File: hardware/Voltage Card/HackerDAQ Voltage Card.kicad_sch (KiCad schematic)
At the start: 21 parts, among them J1 0039301040, J2 0039301040, J3 0039301040, J4 0039301040, J5 0039301040, J6 0039301040, J7 0039301040, J8 0039301040, U2 OPA310xDBV

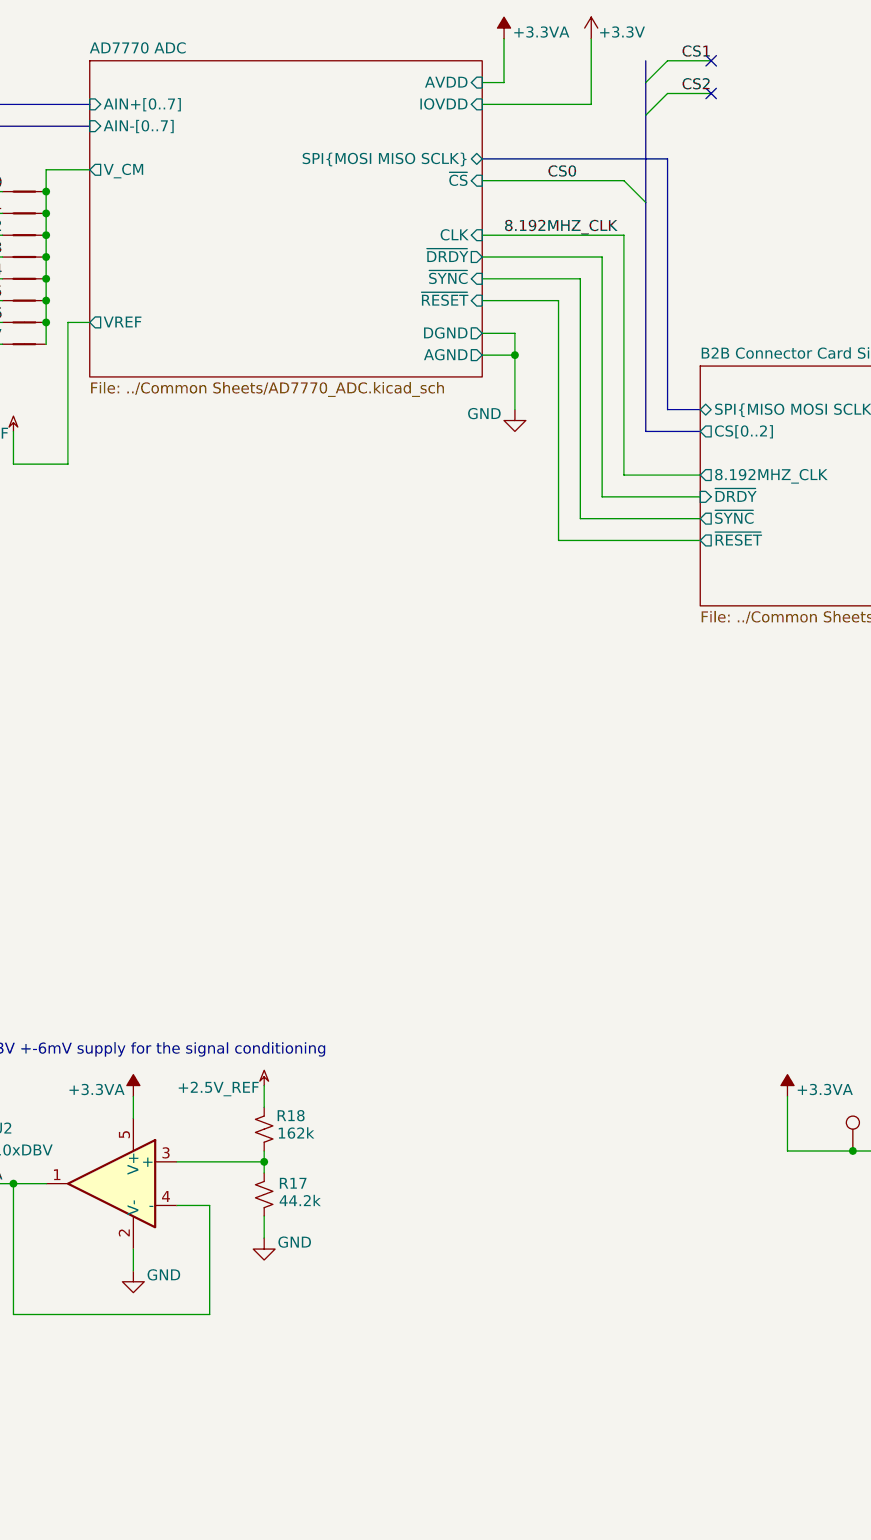
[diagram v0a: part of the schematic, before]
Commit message: Finish initial voltage card design, add logo
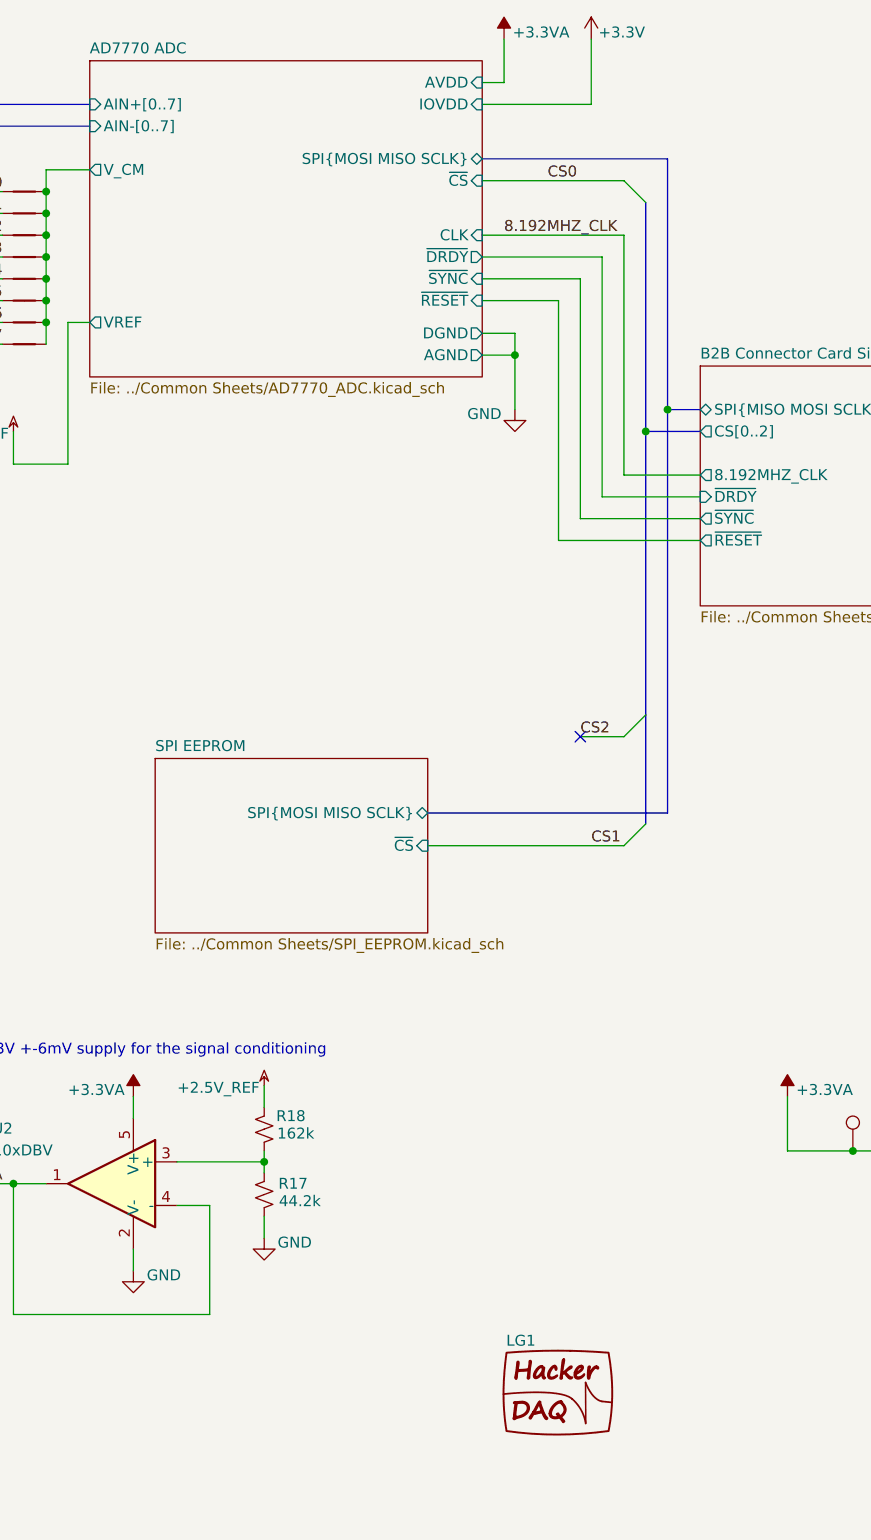
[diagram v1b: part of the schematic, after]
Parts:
- added LG1: ~, Project Library:HackerDAQ Logo, symbol Project Library:HackerDAQ_Logo
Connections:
- no-connect marks 10 -> 9
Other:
- added sheet SPI EEPROM (../Common Sheets/SPI_EEPROM.kicad_sch)
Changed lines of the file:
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@@
 	)
 	(junction
+		(at 196.85 62.23)
+		(diameter 0)
+		(color 0 0 0 0)
+	)
+	(junction
 		(at 123.19 149.86)
 		(diameter 0)
@@
 	)
 	(junction
+		(at 199.39 59.69)
+		(diameter 0)
+		(color 0 0 0 0)
+	)
+	(junction
 		(at 181.61 53.34)
 		(diameter 0)
@@
 	)
 	(no_connect
-		(at 204.47 19.05)
+		(at 189.23 97.79)
 	)
 	(no_connect
@@
 	)
 	(no_connect
-		(at 204.47 22.86)
-	)
-	(no_connect
 		(at 22.86 52.07)
 	)
@@
 	)
 	(bus_entry
-		(at 104.14 133.35)
+		(at 196.85 107.95)
 		(size -2.54 2.54)
 		(stroke
@@
 	)
 	(bus_entry
-		(at 110.49 31.75)
-		(size 2.54 2.54)
+		(at 104.14 133.35)
+		(size -2.54 2.54)
 		(stroke
 			(width 0)
@@
 	)
 	(bus_entry
-		(at 196.85 21.59)
-		(size 2.54 -2.54)
+		(at 110.49 31.75)
+		(size 2.54 2.54)
 		(stroke
 			(width 0)
@@
 	)
 	(bus_entry
-		(at 196.85 25.4)
-		(size 2.54 -2.54)
+		(at 196.85 95.25)
+		(size -2.54 2.54)
 		(stroke
 			(width 0)
@@
 		)
 	)
-	(bus
-		(pts
-			(xy 196.85 21.59) (xy 196.85 25.4)
-		)
-		(stroke
-			(width 0)
-			(type default)
-		)
-	)
 	(wire
 		(pts
@@
 		)
 	)
+	(bus
+		(pts
+			(xy 199.39 59.69) (xy 199.39 106.68)
+		)
+		(stroke
+			(width 0)
+			(type default)
+		)
+	)
 	(wire
 		(pts
@@
 		)
 	)
+	(bus
+		(pts
+			(xy 196.85 95.25) (xy 196.85 107.95)
+		)
+		(stroke
+			(width 0)
+			(type default)
+		)
+	)
 	(wire
 		(pts
@@
 	(bus
 		(pts
-			(xy 196.85 19.05) (xy 196.85 21.59)
-		)
-		(stroke
-			(width 0)
-			(type default)
-		)
-	)
-	(bus
-		(pts
 			(xy 104.14 179.07) (xy 104.14 182.88)
 		)
@@
 	(bus
 		(pts
-			(xy 196.85 25.4) (xy 196.85 35.56)
+			(xy 199.39 59.69) (xy 199.39 30.48)
 		)
 		(stroke
@@
 		)
 	)
-	(bus
+	(wire
 		(pts
-			(xy 199.39 59.69) (xy 199.39 30.48)
+			(xy 194.31 97.79) (xy 189.23 97.79)
 		)
 		(stroke
@@
 		)
 	)
-	(wire
+	(bus
 		(pts
-			(xy 82.55 109.22) (xy 96.52 109.22)
+			(xy 199.39 106.68) (xy 171.45 106.68)
 		)
 		(stroke
@@
 	(wire
 		(pts
-			(xy 254 139.7) (xy 254 149.86)
+			(xy 82.55 109.22) (xy 96.52 109.22)
 		)
 		(stroke
@@
 	(wire
 		(pts
-			(xy 19.05 45.72) (xy 19.05 49.53)
+			(xy 254 139.7) (xy 254 149.86)
 		)
 		(stroke
@@
 	(wire
 		(pts
-			(xy 19.05 135.89) (xy 22.86 135.89)
+			(xy 19.05 45.72) (xy 19.05 49.53)
 		)
 		(stroke
@@
 	(wire
 		(pts
-			(xy 113.03 44.45) (xy 121.92 44.45)
+			(xy 19.05 135.89) (xy 22.86 135.89)
 		)
 		(stroke
@@
 	(wire
 		(pts
-			(xy 199.39 19.05) (xy 204.47 19.05)
+			(xy 113.03 44.45) (xy 121.92 44.45)
 		)
 		(stroke
@@
 		)
 	)
-	(wire
-		(pts
-			(xy 199.39 22.86) (xy 204.47 22.86)
-		)
-		(stroke
-			(width 0)
-			(type default)
-		)
-	)
 	(bus
 		(pts
@@
 	(wire
 		(pts
+			(xy 171.45 110.49) (xy 194.31 110.49)
+		)
+		(stroke
+			(width 0)
+			(type default)
+		)
+	)
+	(wire
+		(pts
 			(xy 152.4 147.32) (xy 152.4 148.59)
 		)
@@
 	(bus
 		(pts
+			(xy 196.85 62.23) (xy 196.85 95.25)
+		)
+		(stroke
+			(width 0)
+			(type default)
+		)
+	)
+	(bus
+		(pts
 			(xy 110.49 41.91) (xy 110.49 44.45)
 		)
@@
 		)
 	)
+	(label "CS2"
+		(at 189.23 97.79 0)
+		(effects
+			(font
+				(size 1.27 1.27)
+			)
+			(justify left bottom)
+		)
+	)
 	(label "AIN-5"
 		(at 121.92 46.99 180)
@@
 		)
 	)
+	(label "CS1"
+		(at 190.5 110.49 0)
+		(effects
+			(font
+				(size 1.27 1.27)
+			)
+			(justify left bottom)
+		)
+	)
 	(label "8.192MHZ_CLK"
 		(at 180.34 39.37 0)
@@
 		)
 	)
-	(label "CS1"
-		(at 204.47 19.05 180)
-		(effects
-			(font
-				(size 1.27 1.27)
-			)
-			(justify right bottom)
-		)
-	)
 	(label "AIN+0"
 		(at 83.82 27.94 0)
@@
 		)
 	)
-	(label "CS2"
-		(at 204.47 22.86 180)
-		(effects
-			(font
-				(size 1.27 1.27)
-			)
-			(justify right bottom)
-		)
-	)
 	(label "CS0"
 		(at 185.42 33.02 0)
@@
 	)
 	(symbol
+		(lib_id "Project Library:HackerDAQ_Logo")
+		(at 184.15 170.18 0)
+		(unit 1)
+		(exclude_from_sim no)
+		(in_bom no)
+		(on_board yes)
+		(dnp no)
+		(property "Reference" "LG1"
+			(at 180.594 168.148 0)
+			(effects
+				(font
+					(size 1.27 1.27)
+				)
+				(justify left)
+			)
+		)
+		(property "Value" "~"
+			(at 184.15 170.18 0)
+			(effects
+				(font
+					(size 1.27 1.27)
+				)
+				(hide yes)
+			)
+		)
+		(property "Footprint" "Project Library:HackerDAQ Logo"
+			(at 195.326 165.1 0)
+			(effects
+				(font
+					(size 1.27 1.27)
+				)
+				(hide yes)
+			)
+		)
+		(property "Datasheet" ""
+			(at 184.15 170.18 0)
+			(effects
+				(font
+					(size 1.27 1.27)
+				)
+				(hide yes)
+			)
+		)
+		(property "Description" ""
+			(at 184.15 170.18 0)
+			(effects
+				(font
+					(size 1.27 1.27)
+				)
+				(hide yes)
+			)
+		)
+		(instances
+			(project ""
+				(path "/af2d881c-6553-449d-9093-6deb41497bdc"
+					(reference "LG1")
+					(unit 1)
+				)
+			)
+		)
+	)
+	(symbol
 		(lib_id "power:GND")
 		(at 39.37 162.56 0)
@@
 				)
 			)
+		)
+	)
+	(sheet
+		(at 139.7 100.33)
+		(size 31.75 20.32)
+		(exclude_from_sim no)
+		(in_bom yes)
+		(on_board yes)
+		(dnp no)
+		(fields_autoplaced yes)
+		(stroke
+			(width 0.1524)
+			(type solid)
+		)
+		(fill
+			(color 0 0 0 0.0000)
+		)
+		(property "Sheetname" "SPI EEPROM"
+			(at 139.7 99.6184 0)
+			(effects
+				(font
+					(size 1.27 1.27)
+				)
+				(justify left bottom)
+			)
+		)
+		(property "Sheetfile" "../Common Sheets/SPI_EEPROM.kicad_sch"
+			(at 139.7 121.2346 0)
+			(effects
+				(font
+					(size 1.27 1.27)
+				)
+				(justify left top)
+			)
+		)
+		(pin "SPI{MOSI MISO SCLK}" bidirectional
+			(at 171.45 106.68 0)
+			(effects
+				(font
+					(size 1.27 1.27)
+				)
+				(justify right)
+			)
+		)
+		(pin "~{CS}" input
+			(at 171.45 110.49 0)
+			(effects
+				(font
+					(size 1.27 1.27)
+				)
+				(justify right)
+			)
+		)
+		(instances
+			(project "HackerDAQ Voltage Card"
+				(path "/af2d881c-6553-449d-9093-6deb41497bdc"
+					(page "13")
+				)
+			)

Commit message: Start on MCU symbol and main unit
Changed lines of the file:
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@@
 		)
 	)
-	(label "CS2"
+	(label "CS1"
 		(at 189.23 97.79 0)
 		(effects
@@
 		)
 	)
-	(label "CS1"
+	(label "CS2"
 		(at 190.5 110.49 0)
 		(effects

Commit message: Main unit: Add USB port for MCU and 3.3VA rail, start on routing
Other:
- sheet 5V To 3.3V LDO ports: added EN; removed none
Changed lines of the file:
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@@
 	)
 	(junction
+		(at 254 147.32)
+		(diameter 0)
+		(color 0 0 0 0)
+	)
+	(junction
 		(at 152.4 147.32)
 		(diameter 0)
@@
 	(wire
 		(pts
+			(xy 254 147.32) (xy 254 149.86)
+		)
+		(stroke
+			(width 0)
+			(type default)
+		)
+	)
+	(wire
+		(pts
 			(xy 96.52 66.04) (xy 96.52 87.63)
 		)
@@
 	(wire
 		(pts
+			(xy 250.19 147.32) (xy 254 147.32)
+		)
+		(stroke
+			(width 0)
+			(type default)
+		)
+	)
+	(wire
+		(pts
 			(xy 152.4 147.32) (xy 142.24 147.32)
 		)
@@
 	(wire
 		(pts
-			(xy 254 139.7) (xy 254 149.86)
+			(xy 254 139.7) (xy 254 147.32)
 		)
 		(stroke
@@
 			)
 		)
+		(pin "EN" input
+			(at 250.19 147.32 0)
+			(effects
+				(font
+					(size 1.27 1.27)
+				)
+				(justify right)
+			)
+		)

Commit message: Route more of main unit, start on KiBot CI job
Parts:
- J1, J2, J3, J4, J5, J6, J7, J8: Mating Connector (none) -> Molex Part #39013045
- renumbered NT5 to NT2, NT2 to NT3, NT6 to NT4, NT3 to NT5, NT7 to NT6, NT4 to NT7, R18 to R17, R17 to R18, TP4 to TP1, TP5 to TP2, U2 to U1
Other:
- sheet SPI EEPROM ports: added V_{CC}; removed none
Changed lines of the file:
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@@
 	(wire
 		(pts
+			(xy 133.35 100.33) (xy 133.35 102.87)
+		)
+		(stroke
+			(width 0)
+			(type default)
+		)
+	)
+	(wire
+		(pts
 			(xy 82.55 22.86) (xy 96.52 22.86)
 		)
@@
 	(wire
 		(pts
+			(xy 133.35 102.87) (xy 139.7 102.87)
+		)
+		(stroke
+			(width 0)
+			(type default)
+		)
+	)
+	(wire
+		(pts
 			(xy 177.8 53.34) (xy 181.61 53.34)
 		)
@@
 			)
 		)
-		(property "Mating Connector" ""
+		(property "Mating Connector" "Molex Part #39013045"
 			(at 30.48 73.66 0)
 			(effects
@@
 		(dnp no)
 		(fields_autoplaced yes)
-		(property "Reference" "NT4"
+		(property "Reference" "NT7"
 			(at 124.46 36.83 0)
 			(effects
@@
 			(project "HackerDAQ Voltage Card"
 				(path "/af2d881c-6553-449d-9093-6deb41497bdc"
-					(reference "NT4")
+					(reference "NT7")
+					(unit 1)
+				)
+			)
+		)
+	)
+	(symbol
+		(lib_id "power:+8V")
+		(at 133.35 100.33 0)
+		(unit 1)
+		(exclude_from_sim no)
+		(in_bom yes)
+		(on_board yes)
+		(dnp no)
+		(property "Reference" "#PWR048"
+			(at 133.35 104.14 0)
+			(effects
+				(font
+					(size 1.27 1.27)
+				)
+				(hide yes)
+			)
+		)
+		(property "Value" "+3.3V"
+			(at 133.35 96.52 0)
+			(effects
+				(font
+					(size 1.27 1.27)
+				)
+			)
+		)
+		(property "Footprint" ""
+			(at 133.35 100.33 0)
+			(effects
+				(font
+					(size 1.27 1.27)
+				)
+				(hide yes)
+			)
+		)
+		(property "Datasheet" ""
+			(at 133.35 100.33 0)
+			(effects
+				(font
+					(size 1.27 1.27)
+				)
+				(hide yes)
+			)
+		)
+		(property "Description" "Power symbol creates a global label with name \"+8V\""
+			(at 133.35 100.33 0)
+			(effects
+				(font
+					(size 1.27 1.27)
+				)
+				(hide yes)
+			)
+		)
+		(pin "1"
+		)
+		(instances
+			(project "HackerDAQ Voltage Card"
+				(path "/af2d881c-6553-449d-9093-6deb41497bdc"
+					(reference "#PWR048")
 					(unit 1)
 				)
@@
 			)
 		)
-		(property "Mating Connector" ""
+		(property "Mating Connector" "Molex Part #39013045"
 			(at 30.48 52.07 0)
 			(effects
@@
 			)
 		)
-		(property "Mating Connector" ""
+		(property "Mating Connector" "Molex Part #39013045"
 			(at 30.48 30.48 0)
 			(effects
@@
 			)
 		)
-		(property "Mating Connector" ""
+		(property "Mating Connector" "Molex Part #39013045"
 			(at 30.48 184.15 0)
 			(effects
@@
 		(dnp no)
 		(fields_autoplaced yes)
-		(property "Reference" "NT7"
+		(property "Reference" "NT6"
 			(at 124.46 44.45 0)
 			(effects
@@
 			(project "HackerDAQ Voltage Card"
 				(path "/af2d881c-6553-449d-9093-6deb41497bdc"
-					(reference "NT7")
+					(reference "NT6")
 					(unit 1)
 				)
@@
 		(dnp no)
 		(fields_autoplaced yes)
-		(property "Reference" "NT6"
+		(property "Reference" "NT4"
 			(at 124.46 41.91 0)
 			(effects
@@
 			(project "HackerDAQ Voltage Card"
 				(path "/af2d881c-6553-449d-9093-6deb41497bdc"
-					(reference "NT6")
+					(reference "NT4")
 					(unit 1)
 				)
@@
 		(on_board yes)
 		(dnp no)
-		(property "Reference" "R17"
+		(property "Reference" "R18"
 			(at 157.48 149.86 0)
 			(effects
@@
 			)
 		)
-		(property "Description" "Resistor 44.2k 0.1% 0.1W 0603"
+		(property "Description" "Resistor, small US symbol"
 			(at 152.4 151.13 0)
 			(effects
@@
 			(project "HackerDAQ Voltage Card"
 				(path "/af2d881c-6553-449d-9093-6deb41497bdc"
-					(reference "R17")
+					(reference "R18")
 					(unit 1)
 				)
@@
 		(dnp no)
 		(fields_autoplaced yes)
-		(property "Reference" "TP4"
+		(property "Reference" "TP1"
 			(at 110.49 153.1619 0)
 			(effects
@@
 			(project "HackerDAQ Voltage Card"
 				(path "/af2d881c-6553-449d-9093-6deb41497bdc"
-					(reference "TP4")
+					(reference "TP1")
 					(unit 1)
 				)
@@
 			)
 		)
-		(property "Mating Connector" ""
+		(property "Mating Connector" "Molex Part #39013045"
 			(at 30.48 116.84 0)
 			(effects
@@
 		(dnp no)
 		(fields_autoplaced yes)
-		(property "Reference" "NT2"
+		(property "Reference" "NT3"
 			(at 124.46 31.75 0)
 			(effects
@@
 			(project "HackerDAQ Voltage Card"
 				(path "/af2d881c-6553-449d-9093-6deb41497bdc"
-					(reference "NT2")
+					(reference "NT3")
 					(unit 1)
 				)
@@
 		(dnp no)
 		(fields_autoplaced yes)
-		(property "Reference" "NT3"
+		(property "Reference" "NT5"
 			(at 124.46 34.29 0)
 			(effects
@@
 			(project "HackerDAQ Voltage Card"
 				(path "/af2d881c-6553-449d-9093-6deb41497bdc"
-					(reference "NT3")
+					(reference "NT5")
 					(unit 1)
 				)
@@
 		(dnp no)
 		(fields_autoplaced yes)
-		(property "Reference" "TP5"
+		(property "Reference" "TP2"
 			(at 223.52 141.4779 0)
 			(effects
@@
 			(project "HackerDAQ Voltage Card"
 				(path "/af2d881c-6553-449d-9093-6deb41497bdc"
-					(reference "TP5")
+					(reference "TP2")
 					(unit 1)
 				)
@@
 			)
 		)
-		(property "Mating Connector" ""
+		(property "Mating Connector" "Molex Part #39013045"
 			(at 30.48 160.02 0)
 			(effects
@@
 			)
 		)
-		(property "Mating Connector" ""
+		(property "Mating Connector" "Molex Part #39013045"
 			(at 30.48 138.43 0)
 			(effects
@@
 			)
 		)
-		(property "Mating Connector" ""
+		(property "Mating Connector" "Molex Part #39013045"
 			(at 30.48 95.25 0)
 			(effects
@@
 		(on_board yes)
 		(dnp no)
-		(property "Reference" "R18"
+		(property "Reference" "R17"
 			(at 157.226 141.986 0)
 			(effects
@@
 			)
 		)
-		(property "Description" "Resistor 162k 0.1% 0.1W 0603"
+		(property "Description" "Resistor, small US symbol"
 			(at 152.4 143.51 0)
 			(effects
@@
 			(project "HackerDAQ Voltage Card"
 				(path "/af2d881c-6553-449d-9093-6deb41497bdc"
-					(reference "R18")
+					(reference "R17")
 					(unit 1)
 				)
@@
 		(dnp no)
 		(fields_autoplaced yes)
-		(property "Reference" "U2"
+		(property "Reference" "U1"
 			(at 121.92 143.4398 0)
 			(effects
@@
 			)
 		)
-		(property "Description" "Opamp, 1.5-5.5V supply, +-150mA current, +-0.25mV offset voltage"
+		(property "Description" "High output current, Rail-to-Rail Input/Output, 3MHz GBW, Operational Amplifiers, integrated RFI/EMI filter, 1.5V to 5.5V supply, SOT-23-5"
 			(at 134.62 149.86 0)
 			(effects
@@
 			(project ""
 				(path "/af2d881c-6553-449d-9093-6deb41497bdc"
-					(reference "U2")
+					(reference "U1")
 					(unit 1)
 				)
@@
 		(dnp no)
 		(fields_autoplaced yes)
-		(property "Reference" "NT5"
+		(property "Reference" "NT2"
 			(at 124.46 39.37 0)
 			(effects
@@
 			(project "HackerDAQ Voltage Card"
 				(path "/af2d881c-6553-449d-9093-6deb41497bdc"
-					(reference "NT5")
+					(reference "NT2")
 					(unit 1)
 				)
@@
 			)
 		)
+		(pin "V_{CC}" input
+			(at 139.7 102.87 180)
+			(effects
+				(font
+					(size 1.27 1.27)
+				)
+				(justify left)
+			)
+		)

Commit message: Add Main Unit to CI build as well
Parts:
- R17: LibRef (none) -> RT0603BRD07162KL
- R18: LibRef (none) -> RT0603BRD0744K2L
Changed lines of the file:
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@@
+			)
+		)
+		(property "LibRef" "RT0603BRD0744K2L"
+			(at 152.4 151.13 0)
+			(effects
+				(font
+					(size 1.27 1.27)
+				)
+				(hide yes)
 			)
 		)
@@
 			(at 152.4 143.51 0)
 			(effects
+				(font
+					(size 1.27 1.27)
+				)
+				(hide yes)
+			)
+		)
+		(property "LibRef" "RT0603BRD07162KL"
+			(at 152.4 143.51 0)
+			(effects
